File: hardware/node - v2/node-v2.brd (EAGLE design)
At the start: 83.2 x 53.3 mm, 54 parts, among them IC1 HYPERTRIANGLE_TCS3472FN, Q1 32.768kHz, Q2 24MHz, U1 INA322_DGK_8, U2 LMV551_DBV_5, X1 BU-SMA-1-7HOLE

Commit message: NODEHW: Further updates to capacitor values found as part of #6
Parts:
- C2: value 10n -> 1u
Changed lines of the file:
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@@
 <elements>
 <element name="C1" library="SparkFun-Capacitors" package="CAP-PTH-SMALL" value="1n" x="59.4675" y="29.186" rot="R90"/>
-<element name="C2" library="SparkFun-Capacitors" package="CAP-PTH-SMALL" value="10n" x="73.0685" y="32.843" rot="R270"/>
+<element name="C2" library="SparkFun-Capacitors" package="CAP-PTH-SMALL" value="1u" x="73.0685" y="32.843" rot="R270"/>
 <element name="C3" library="SparkFun-Capacitors" package="CPOL-RADIAL-10UF-25V" value="10u" x="71.208" y="36.2435" rot="R90"/>
 <element name="R1" library="resistor" package="0204/7" value="10k" x="62.5235" y="22.545" rot="R270"/>

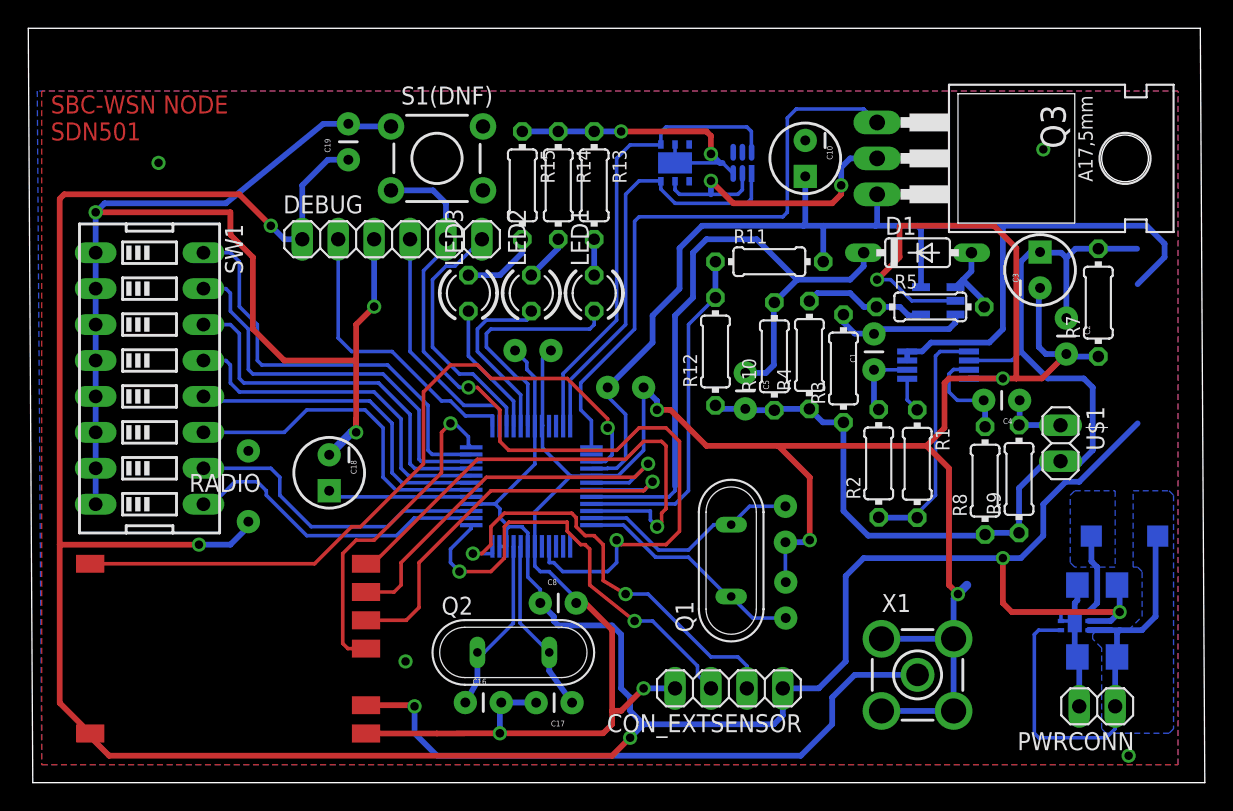
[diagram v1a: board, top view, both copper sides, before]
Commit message: NODEHW: Completed v2 rework. There are no ADC pins available for #9 therefore it is wontfix.
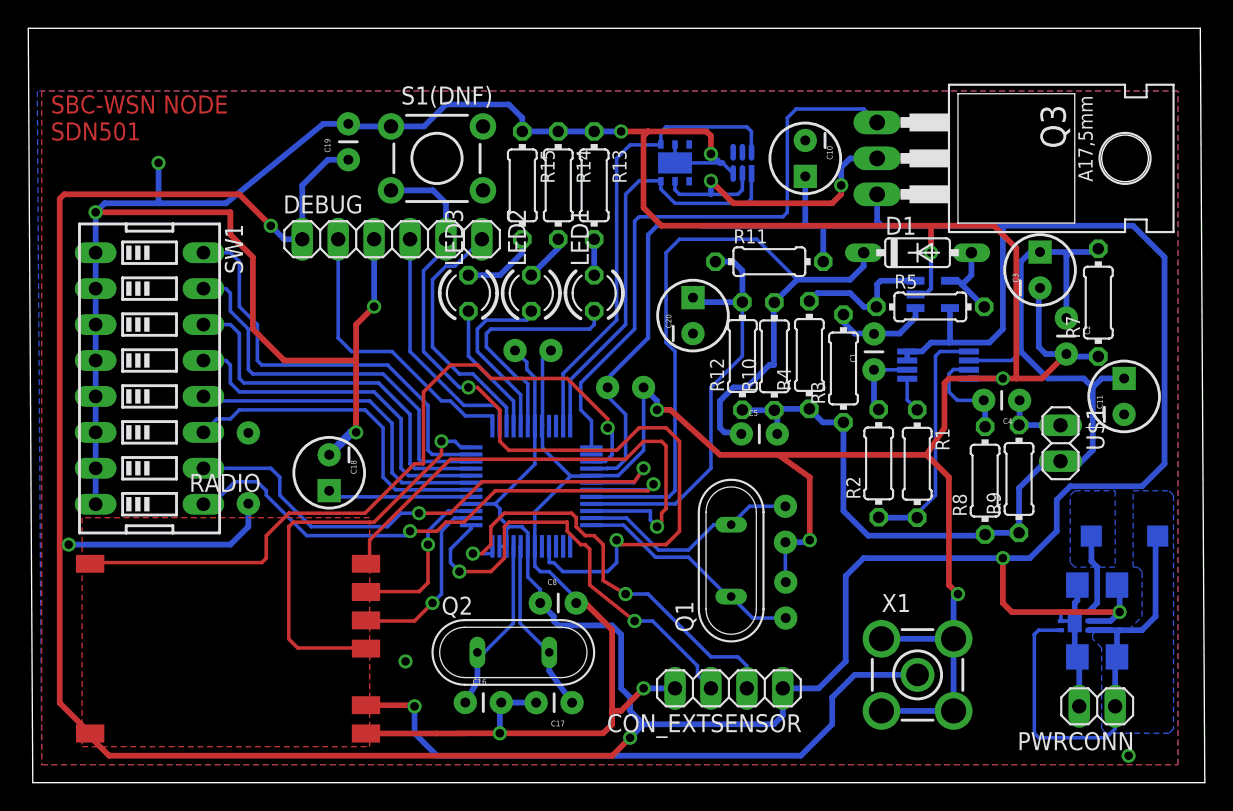
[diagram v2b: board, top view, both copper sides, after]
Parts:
- added C11: 10u, SparkFun-Capacitors:CPOL-RADIAL-10UF-25V
- added C20: 100u, SparkFun-Capacitors:CPOL-RADIAL-10UF-25V
- moved C5 4.32 mm to (50.1, 24.7), turned to 0 degrees
- moved R12 1.93 mm to (50.2, 30.2)
- moved C7 1.27 mm to (15.2, 22.2)
- moved U2 0.60 mm to (63.6, 34.5), turned to 180 degrees
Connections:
- removed net RADIO_MISO: RADIO.MISO, U$2.7
- new net N$1: RADIO.MISO, U$2.26
- net DETECT_REF: now also C20.1
- net GND: now also C11.2, C20.2
- net INSTR_FILTERED: now also U2.1; no longer U2.3
- net OPAMP_OUT: now also U2.4; no longer U2.1
- net OPAMP_VGND: now also U2.3; no longer U2.4
- net RADIO_MOSI: now also U$2.27; no longer U$2.6
- net SW_ADDR_7: now also U$2.6; no longer U$2.27
- net SW_ADDR_8: now also U$2.7; no longer U$2.26
- net VCC/2: now also C11.1
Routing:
- net GND: track 309.5 -> 341.5 mm, vias 16 -> 15
- net RADIO_MISO: track 30.7 -> 0.00 mm, vias 1 -> 0
- net SW_ADDR_8: track 21.9 -> 40.3 mm, vias 0 -> 2
- net SW_ADDR_7: track 21.8 -> 39.6 mm, vias 0 -> 2
- net RADIO_MOSI: track 29.2 -> 11.9 mm
- net +3V3: track 312.5 -> 325.8 mm
- net N$1: track 0.00 -> 13.1 mm, vias 0 -> 1
- net DETECT_OUT: track 47.7 -> 55.6 mm
- net RADIO_SCK: track 23.7 -> 29.8 mm
- net DETECT_REF: track 24.2 -> 30.2 mm
- net INSTR_FILTERED: track 9.71 -> 7.13 mm
- net RADIO_CS: track 36.4 -> 37.7 mm
- net OPAMP_VGND: track 8.82 -> 9.82 mm
- net RADIO_INT: track 51.3 -> 52.2 mm
- added copper zone on layer 1, net N$2
